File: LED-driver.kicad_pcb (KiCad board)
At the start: 2 copper layers, 60.1 x 81.9 mm, 38 parts, among them J1 Screw_Terminal_1x02, J2 PIC Kit3 header, J3 Screw_Terminal_1x02, J4 Screw_Terminal_1x02, J5 Screw_Terminal_1x02, J6 Screw_Terminal_1x03, Q1 Q_NMOS_DGS, Q2 Q_NMOS_DGS, Q3 Q_NMOS_DGS, U1 PIC12F1572, U2 CAT4101, U3 MAX485, U4 CAT4101, U5 CAT4101

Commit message: Various tweaks and Gerber export.
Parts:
- moved 10K 13.4 mm to (161.7, 84.1), turned to 0 degrees
- moved 10K 6.13 mm to (167.5, 69.7)
- moved 0.1uF4 2.92 mm to (172.6, 79.9)
- moved J6 2.92 mm to (181.0, 83.8)
- moved 10K 2.92 mm to (161.7, 77.0)
- moved U3 2.92 mm to (167.4, 76.2)
- moved Q3 2.67 mm to (161.5, 73.3)
- renumbered 10K1 to 10K, 10K5 to 10K, 10K6 to 10K, 510R1 to 510R, 510R2 to 510R, 510R3 to 510R, U2 to CAT4101, U4 to CAT4101, U5 to CAT4101, D3 to LED, JP1 to MCLR, JP2 to RX, JP3 to TX
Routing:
- net GND: track 108.3 -> 113.1 mm
- net Net-(JP2-Pad2): track 26.5 -> 29.4 mm
- net Net-(10K1-Pad2): track 24.0 -> 26.5 mm
- net Net-(U1-Pad3): track 28.0 -> 25.7 mm
- net +5V: track 290.3 -> 288.0 mm
- net Net-(10K5-Pad2): track 42.4 -> 41.4 mm
- net Net-(10K5-Pad1): track 5.06 -> 4.20 mm
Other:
- board text added: "Designed by James Hanlon"
- board text added: "LED driver"
- board text added: "jwhanlon.com"

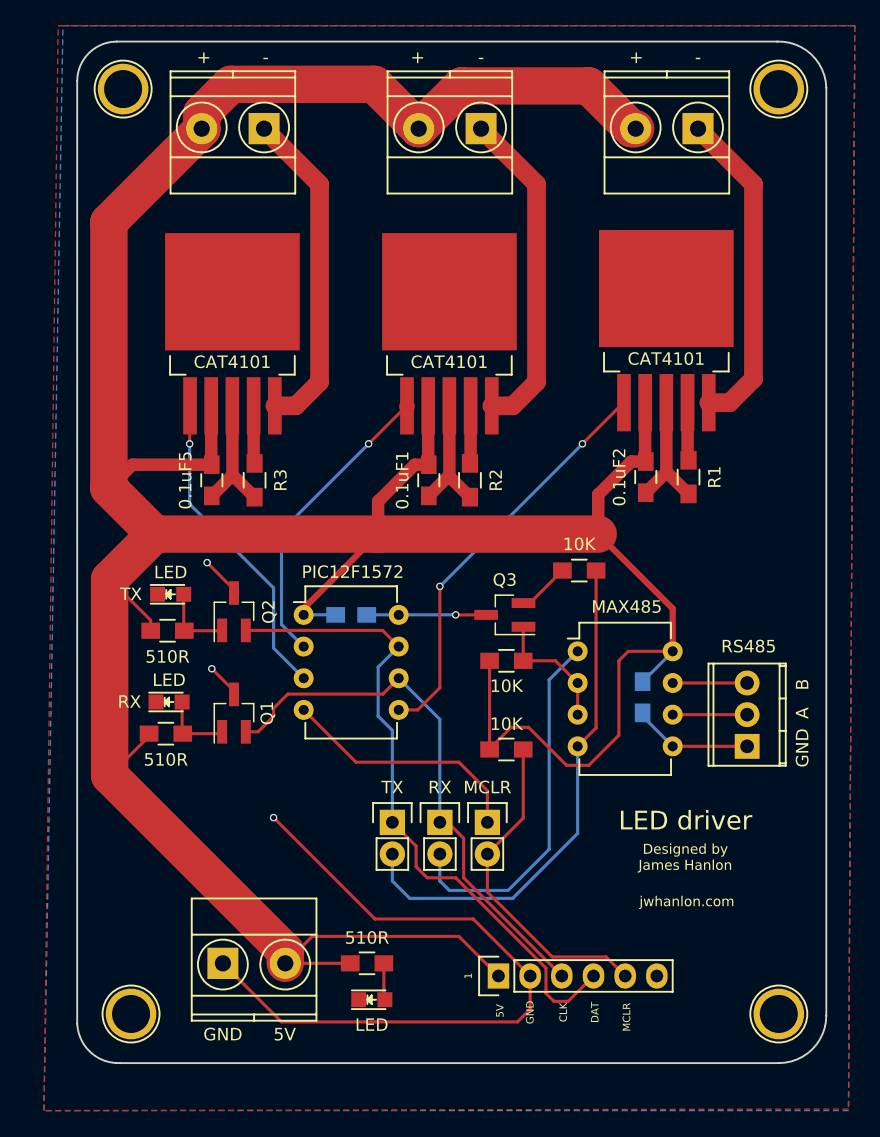
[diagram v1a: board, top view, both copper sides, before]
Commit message: Fix schematic-PCB references and update GBR files.
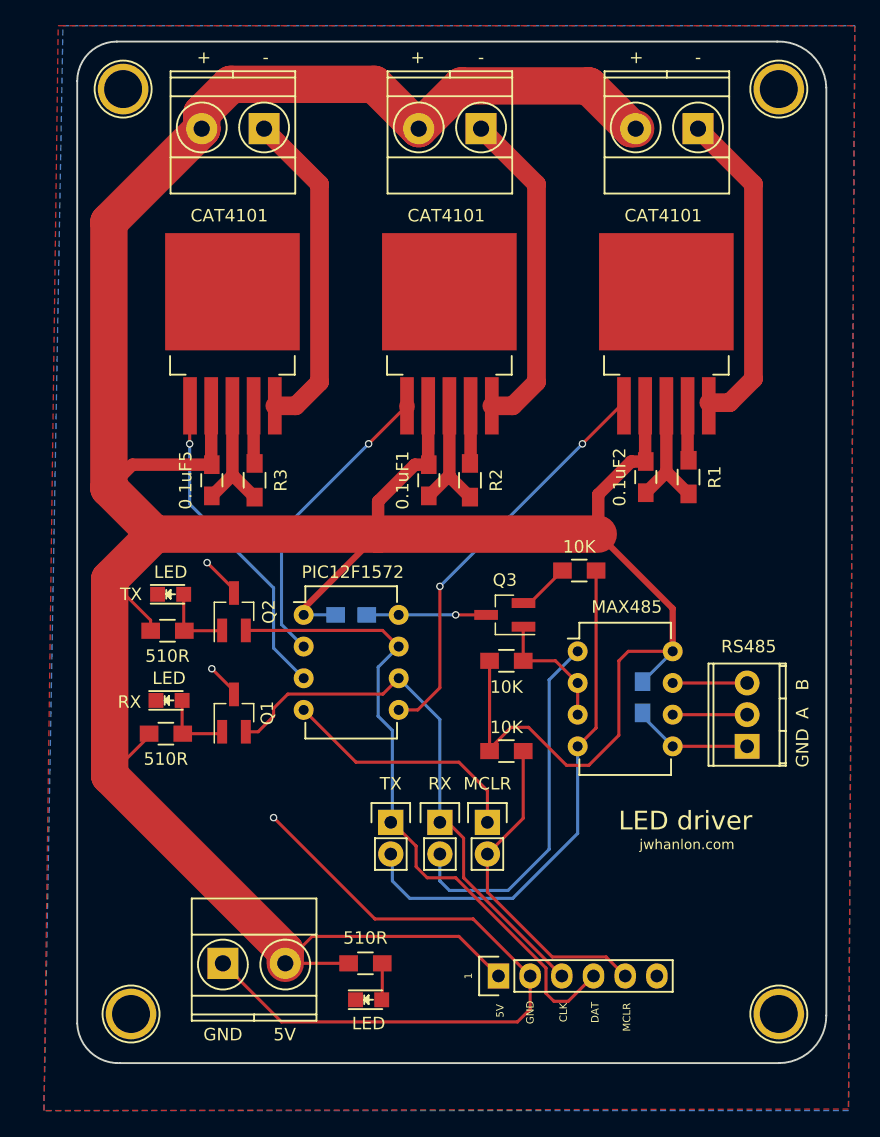
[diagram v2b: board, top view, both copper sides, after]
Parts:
- removed 10K (x3), 510R (x3): R, Resistors_SMD:R_0805_HandSoldering
- removed CAT4101 (x3): CAT4101, TO_SOT_Packages_SMD:TO-263-5Lead
- removed LED (x2): LED, LEDs:LED_0805
- removed MCLR: Jumper_NC_Small, Pin_Headers:Pin_Header_Straight_1x02
- removed RX, TX: Jumper_NO_Small, Pin_Headers:Pin_Header_Straight_1x02
- added D1: LED, LEDs:LED_0805, F.Cu at (134.6, 80.1)
- added D2: LED, LEDs:LED_0805, F.Cu at (150.6, 104.1)
- added JP1: MCLR, Pin_Headers:Pin_Header_Straight_1x02, F.Cu at (160.1, 89.9)
- added JP2: RX, Pin_Headers:Pin_Header_Straight_1x02, F.Cu at (156.3, 89.9)
- added JP3: TX, Pin_Headers:Pin_Header_Straight_1x02, F.Cu at (152.4, 89.9)
- added R4: 510R, Resistors_SMD:R_0805_HandSoldering, F.Cu at (134.4, 82.8)
- added R5: 510R, Resistors_SMD:R_0805_HandSoldering, F.Cu at (134.5, 74.5)
- added R6: 510R, Resistors_SMD:R_0805_HandSoldering, F.Cu at (150.4, 101.2)
- added R7: 10K, Resistors_SMD:R_0805_HandSoldering, F.Cu at (161.7, 84.2)
- added R8: 10K, Resistors_SMD:R_0805_HandSoldering, F.Cu at (167.5, 69.7)
- added R9: 10K, Resistors_SMD:R_0805_HandSoldering, F.Cu at (161.7, 77.0)
- added U2: CAT4101, TO_SOT_Packages_SMD:TO-263-5Lead, F.Cu at (174.5, 56.5)
- added U4: CAT4101, TO_SOT_Packages_SMD:TO-263-5Lead, F.Cu at (157.1, 56.5)
- added U5: CAT4101, TO_SOT_Packages_SMD:TO-263-5Lead, F.Cu at (139.7, 56.5)
- renumbered LED to D3
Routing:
- net Net-(D2-Pad2): track 0.00 -> 3.05 mm
- net Net-(510R3-Pad2): track 2.95 -> 0.00 mm
- net GND: track 113.1 -> 112.0 mm
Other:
- board text removed: "Designed by James Hanlon"

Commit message: Tweaks to vias.
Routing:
- net GND: track 112.0 -> 121.9 mm
- net Net-(JP3-Pad2): track 41.4 -> 48.5 mm
- net Net-(Q3-Pad1): track 10.4 -> 15.5 mm
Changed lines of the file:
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@@
     (thickness 1.6)
     (drawings 32)
-    (tracks 209)
+    (tracks 221)
     (zones 0)
     (modules 38)
@@
   (segment (start 172.798 60.931) (end 172.847 60.98) (width 1) (layer F.Cu) (net 1) (status 30))
   (segment (start 172.038 34.036) (end 171.958 34.036) (width 1.25) (layer B.Cu) (net 1) (status 30))
+  (segment (start 175.006 83.82) (end 172.339 83.82) (width 0.25) (layer B.Cu) (net 2))
+  (via (at 166.497 72.263) (size 0.6) (drill 0.4) (layers F.Cu B.Cu) (net 2))
+  (segment (start 169.291 75.057) (end 166.497 72.263) (width 0.25) (layer B.Cu) (net 2))
+  (segment (start 169.291 80.772) (end 169.291 75.057) (width 0.25) (layer B.Cu) (net 2))
+  (segment (start 172.339 83.82) (end 169.291 80.772) (width 0.25) (layer B.Cu) (net 2))
+  (segment (start 139.827 71.525) (end 138.835 71.525) (width 0.25) (layer F.Cu) (net 2))
+  (via (at 137.668 70.358) (size 0.6) (drill 0.4) (layers F.Cu B.Cu) (net 2))
+  (segment (start 138.835 71.525) (end 137.668 70.358) (width 0.25) (layer F.Cu) (net 2))
+  (segment (start 139.827 79.653) (end 139.724 79.653) (width 0.25) (layer F.Cu) (net 2))
+  (segment (start 139.724 79.653) (end 137.541 77.47) (width 0.25) (layer F.Cu) (net 2))
+  (via (at 137.541 77.47) (size 0.6) (drill 0.4) (layers F.Cu B.Cu) (net 2))
   (segment (start 172.593 81.133) (end 172.593 81.407) (width 0.25) (layer B.Cu) (net 2) (status 30))
   (segment (start 172.593 81.407) (end 175.006 83.82) (width 0.25) (layer B.Cu) (net 2) (status 30))
   (segment (start 180.975 83.82) (end 175.006 83.82) (width 0.25) (layer F.Cu) (net 2) (status 30))
-  (segment (start 160.044 73.279) (end 157.607 73.279) (width 0.25) (layer F.Cu) (net 2) (status 10))
-  (via (at 157.607 73.279) (size 0.6) (drill 0.4) (layers F.Cu B.Cu) (net 2))
-  (segment (start 157.607 73.279) (end 153.035 73.279) (width 0.25) (layer B.Cu) (net 2) (status 20))
   (segment (start 139.827 79.653) (end 139.827 79.375) (width 0.25) (layer F.Cu) (net 2) (status 30))
-  (segment (start 139.827 79.375) (end 138.049 77.597) (width 0.25) (layer F.Cu) (net 2) (status 10))
-  (via (at 138.049 77.597) (size 0.6) (drill 0.4) (layers F.Cu B.Cu) (net 2))
   (segment (start 139.827 71.525) (end 139.827 71.247) (width 0.25) (layer F.Cu) (net 2) (status 30))
-  (segment (start 139.827 71.247) (end 137.668 69.088) (width 0.25) (layer F.Cu) (net 2) (status 10))
-  (via (at 137.668 69.088) (size 0.6) (drill 0.4) (layers F.Cu B.Cu) (net 2))
   (segment (start 163.576 102.235) (end 159.004 97.663) (width 0.25) (layer F.Cu) (net 2) (status 10))
   (via (at 143.002 89.535) (size 0.6) (drill 0.4) (layers F.Cu B.Cu) (net 2))
@@
   (segment (start 163.021 84.074) (end 163.021 89.582) (width 0.25) (layer F.Cu) (net 22) (status 10))
   (segment (start 163.021 89.582) (end 160.147 92.456) (width 0.25) (layer F.Cu) (net 22) (status 20))
-  (segment (start 168.863 69.723) (end 168.863 82.343) (width 0.25) (layer F.Cu) (net 23) (status 10))
-  (segment (start 168.863 82.343) (end 167.386 83.82) (width 0.25) (layer F.Cu) (net 23) (status 20))
+  (segment (start 167.386 83.82) (end 170.053 81.153) (width 0.25) (layer F.Cu) (net 23))
+  (segment (start 170.942 69.723) (end 168.863 69.723) (width 0.25) (layer F.Cu) (net 23))
+  (segment (start 174.371 73.152) (end 170.942 69.723) (width 0.25) (layer F.Cu) (net 23))
+  (segment (start 174.371 74.608998) (end 174.371 73.152) (width 0.25) (layer F.Cu) (net 23))
+  (segment (start 173.287998 75.692) (end 174.371 74.608998) (width 0.25) (layer F.Cu) (net 23))
+  (segment (start 171.196 75.692) (end 173.287998 75.692) (width 0.25) (layer F.Cu) (net 23))
+  (segment (start 170.053 76.835) (end 171.196 75.692) (width 0.25) (layer F.Cu) (net 23))
+  (segment (start 170.053 81.153) (end 170.053 76.835) (width 0.25) (layer F.Cu) (net 23))
   (segment (start 167.386 83.82) (end 167.386 90.805) (width 0.25) (layer B.Cu) (net 23) (status 10))
   (segment (start 152.527 94.615) (end 153.924 96.012) (width 0.25) (layer B.Cu) (net 23))
@@
   (segment (start 162.179 96.012) (end 167.386 90.805) (width 0.25) (layer B.Cu) (net 23))
   (segment (start 152.527 94.615) (end 152.527 92.456) (width 0.25) (layer B.Cu) (net 23) (status 20))
+  (segment (start 167.386 81.28) (end 165.354 83.312) (width 0.25) (layer F.Cu) (net 24))
+  (segment (start 163.021 81.106) (end 163.021 76.962) (width 0.25) (layer F.Cu) (net 24))
+  (segment (start 165.227 83.312) (end 163.021 81.106) (width 0.25) (layer F.Cu) (net 24))
+  (segment (start 165.354 83.312) (end 165.227 83.312) (width 0.25) (layer F.Cu) (net 24))
   (segment (start 163.021 76.962) (end 163.021 74.252) (width 0.25) (layer F.Cu) (net 24) (status 30))
   (segment (start 163.021 74.252) (end 163.044 74.229) (width 0.25) (layer F.Cu) (net 24) (status 30))
   (segment (start 167.386 81.28) (end 167.386 78.74) (width 0.25) (layer F.Cu) (net 24) (status 30))
-  (segment (start 163.021 76.962) (end 165.608 76.962) (width 0.25) (layer F.Cu) (net 24) (status 10))
-  (segment (start 165.608 76.962) (end 167.386 78.74) (width 0.25) (layer F.Cu) (net 24) (status 20))
   (segment (start 163.044 72.329) (end 163.557 72.329) (width 0.25) (layer F.Cu) (net 25) (status 30))
   (segment (start 163.557 72.329) (end 166.163 69.723) (width 0.25) (layer F.Cu) (net 25) (status 30))

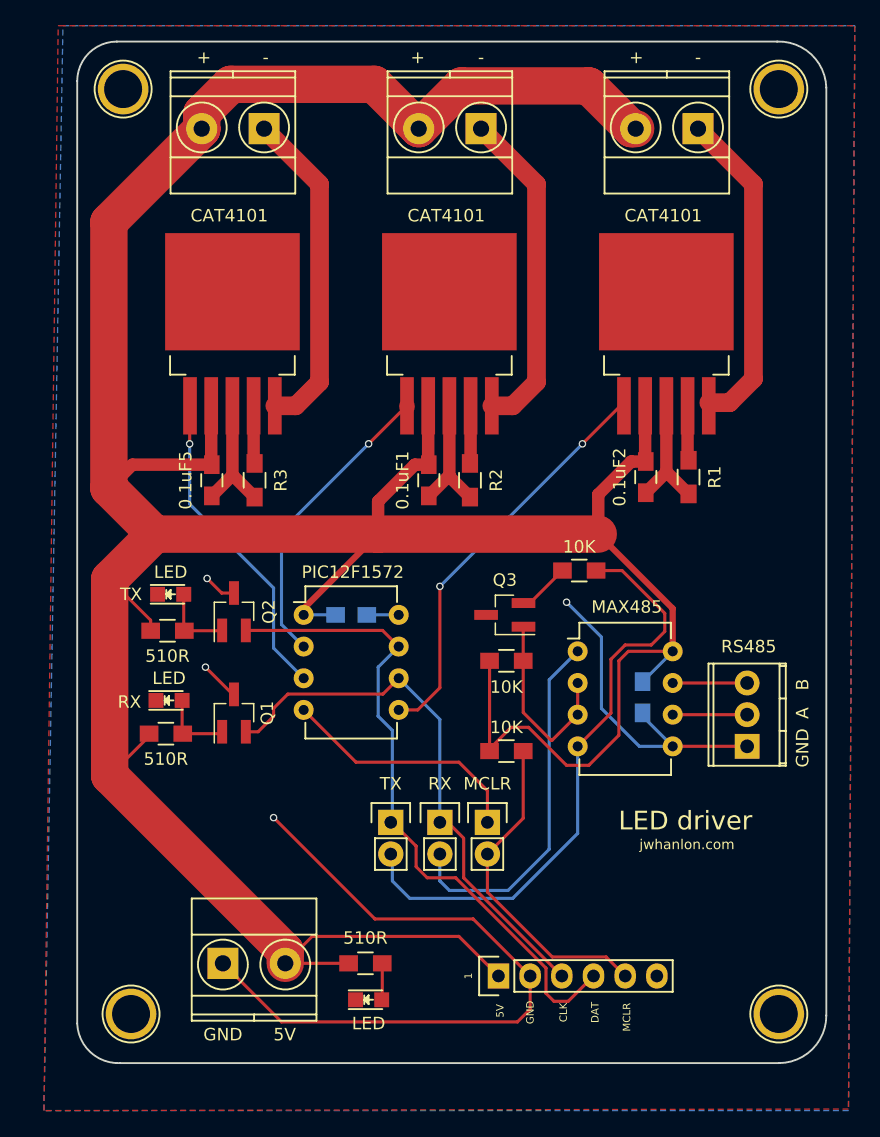
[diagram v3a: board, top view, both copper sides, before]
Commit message: Tweak resistor values.
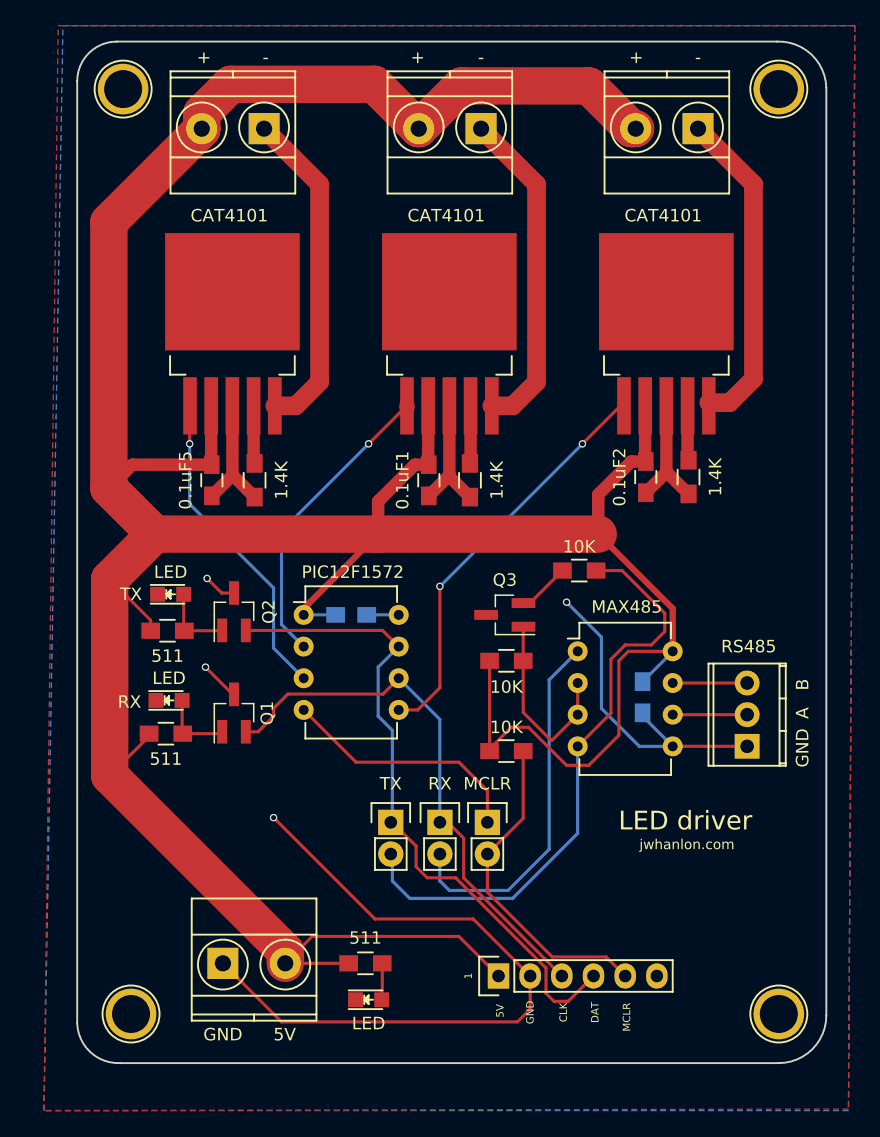
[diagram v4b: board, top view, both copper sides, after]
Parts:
- R1, R2, R3: value R_Small -> 1.4K
- R4, R5, R6: value 510R -> 511
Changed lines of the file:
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@@
     (tags "resistor 0805")
     (attr smd)
-    (fp_text reference R1 (at 0 -2.1 270) (layer F.SilkS)
-      (effects (font (size 1 1) (thickness 0.15)))
-    )
-    (fp_text value R_Small (at 0 2.1 270) (layer F.Fab) hide
+    (fp_text reference R1 (at 0 -2.1 270) (layer F.SilkS) hide
+      (effects (font (size 1 1) (thickness 0.15)))
+    )
+    (fp_text value 1.4K (at 0 -2.159 270) (layer F.SilkS)
       (effects (font (size 1 1) (thickness 0.15)))
     )
@@
     (tags "resistor 0805")
     (attr smd)
-    (fp_text reference R2 (at 0 -2.1 270) (layer F.SilkS)
-      (effects (font (size 1 1) (thickness 0.15)))
-    )
-    (fp_text value R_Small (at 0 2.1 270) (layer F.Fab) hide
+    (fp_text reference R2 (at 0 -2.1 270) (layer F.SilkS) hide
+      (effects (font (size 1 1) (thickness 0.15)))
+    )
+    (fp_text value 1.4K (at 0 -2.159 270) (layer F.SilkS)
       (effects (font (size 1 1) (thickness 0.15)))
     )
@@
     (tags "resistor 0805")
     (attr smd)
-    (fp_text reference R3 (at 0 -2.1 270) (layer F.SilkS)
-      (effects (font (size 1 1) (thickness 0.15)))
-    )
-    (fp_text value R_Small (at 0 2.1 270) (layer F.Fab) hide
+    (fp_text reference R3 (at 0 -2.1 270) (layer F.SilkS) hide
+      (effects (font (size 1 1) (thickness 0.15)))
+    )
+    (fp_text value 1.4K (at 0 -2.159 270) (layer F.SilkS)
       (effects (font (size 1 1) (thickness 0.15)))
     )
@@
       (effects (font (size 1 1) (thickness 0.15)))
     )
-    (fp_text value 510R (at 0 -2.032 180) (layer F.SilkS)
+    (fp_text value 511 (at 0 -2.032 180) (layer F.SilkS)
       (effects (font (size 1 1) (thickness 0.15)))
     )
@@
       (effects (font (size 1 1) (thickness 0.15)))
     )
-    (fp_text value 510R (at 0 -2.032 180) (layer F.SilkS)
+    (fp_text value 511 (at 0 -2.032 180) (layer F.SilkS)
       (effects (font (size 1 1) (thickness 0.15)))
     )
@@
       (effects (font (size 1 1) (thickness 0.15)))
     )
-    (fp_text value 510R (at 0 -2.032) (layer F.SilkS)
-      (effects (font (size 1 1) (thickness 0.15)))
-    )
+    (fp_text value 511 (at 0 -2.032) (layer F.SilkS)
+      (effects (font (size 1 1) (thickness 0.15)))
+    )

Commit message: Final tweaks.
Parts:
- 0.1uF1, 0.1uF2, 0.1uF3, 0.1uF4, 0.1uF5: value CP -> 0.1uF
- Q1, Q2: value Q_NMOS_DGS -> 2N7002
- Q3: value Q_NMOS_DGS -> BSS123
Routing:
- net Net-(JP3-Pad2): track 48.5 -> 46.6 mm
- net UART_RX/CLK: track 44.1 -> 45.1 mm
- net GND: track 121.9 -> 122.7 mm
